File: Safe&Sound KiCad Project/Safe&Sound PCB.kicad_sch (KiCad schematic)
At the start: 14 parts

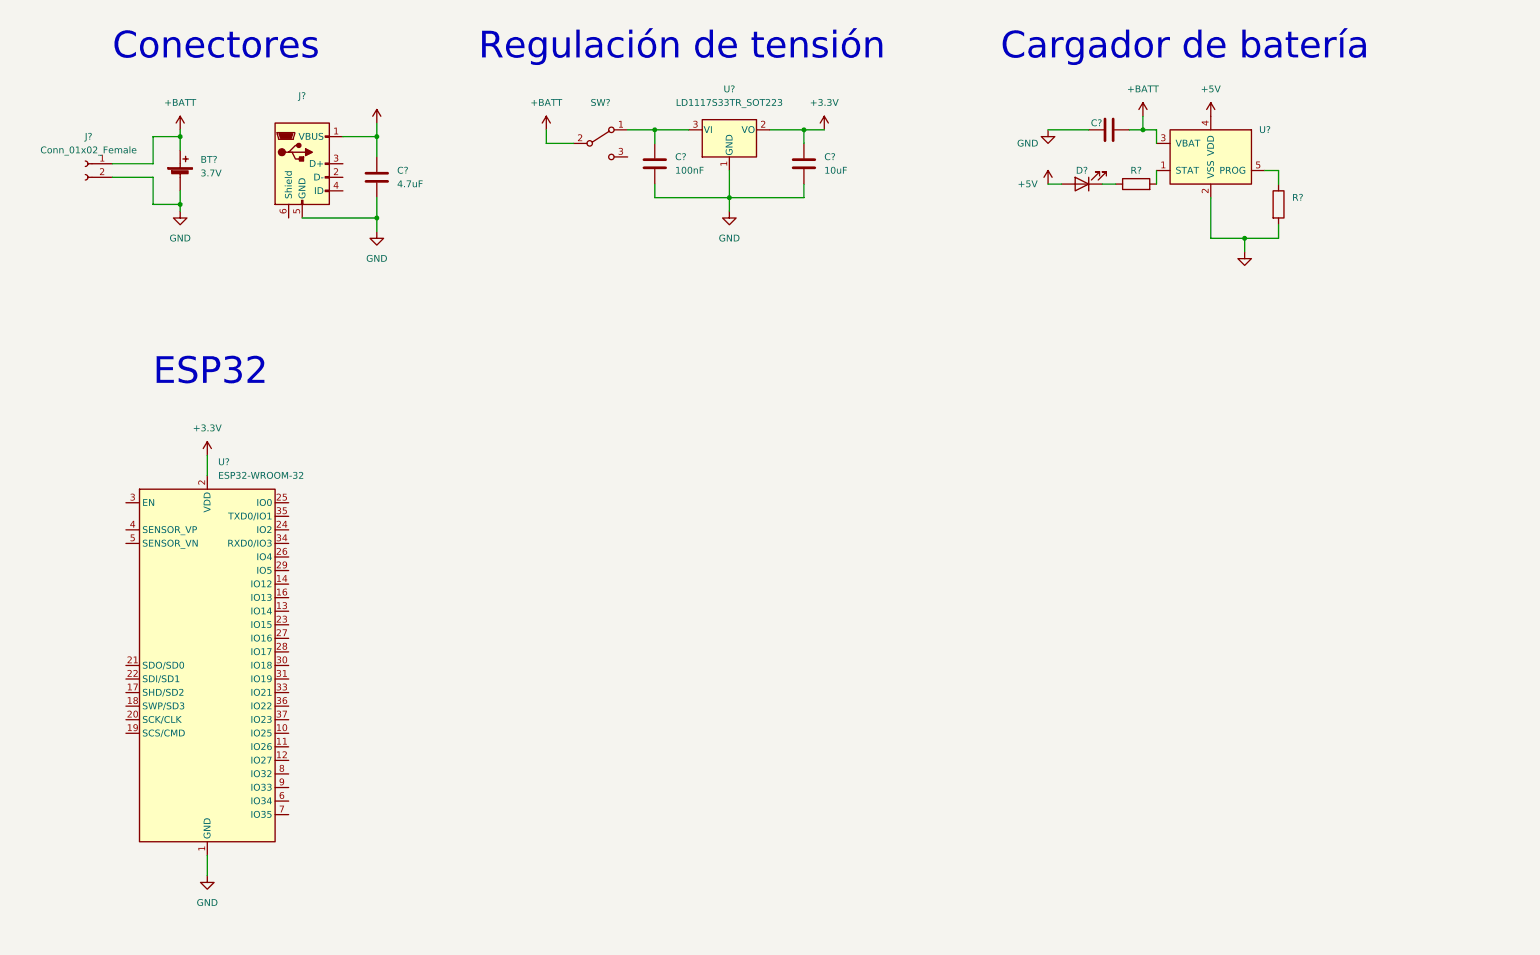
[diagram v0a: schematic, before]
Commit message: Puerto de programación
- Se añade un socket para hacer uso de un módulo USB a TTL con CP2102 para la programación del módulo ESP32-WROOM-32.
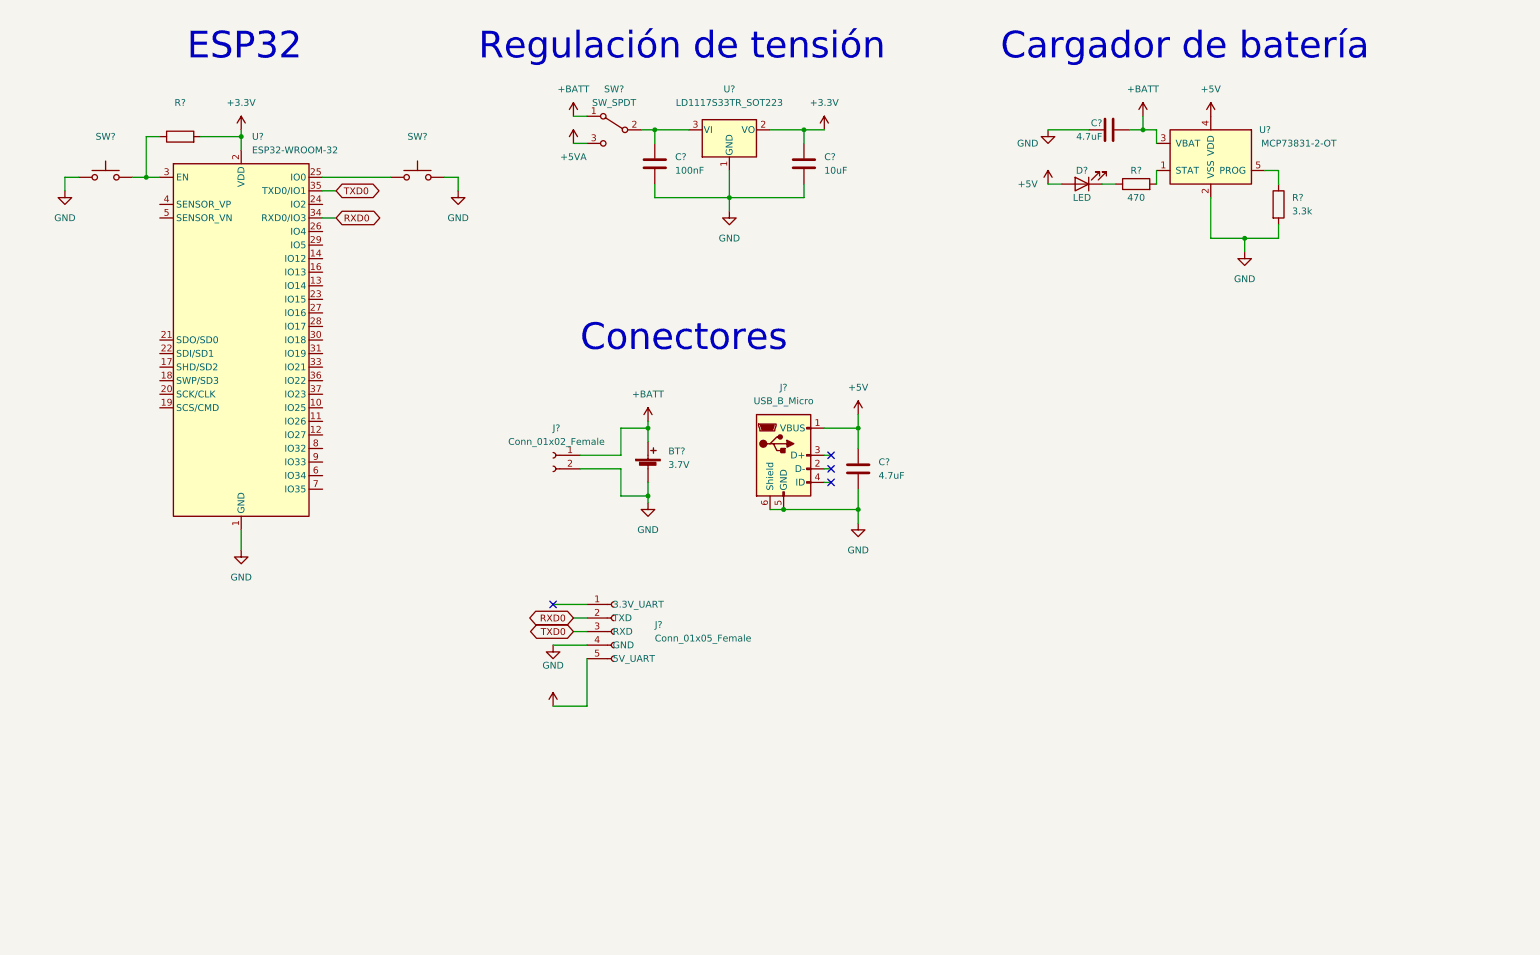
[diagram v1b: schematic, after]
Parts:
- added J?: Conn_01x05_Female, Connector_PinSocket_2.54mm:PinSocket_1x05_P2.54mm_Horizontal, symbol Connector:Conn_01x05_Female
- added R?: (no value), symbol Device:R
- added SW? (x2): (no value), symbol Switch:SW_Push
- C?: value (none) -> 4.7uF
- D?: value (none) -> LED
- J?: value (none) -> USB_B_Micro
- R?: value (none) -> 3.3k
- R?: value (none) -> 470
- SW?: value (none) -> SW_SPDT
- U?: value (none) -> MCP73831-2-OT; footprint (none) -> Package_TO_SOT_SMD:SOT-23-5
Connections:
- net +3V3: now also R?.2
- net +BATT: now also SW?.1 (A); no longer SW?.2 (B)
- net GND: now also J?.6 (Shield), J?.4 (GND), SW?.1, SW?.2
- net at U?.25 (IO0): now also SW?.1
- net at U?.3 (EN): now also R?.1, SW?.2
- net RXD0: now reaches U?.34 (RXD0/IO3)
- net RXD0: now also J?.2 (TXD)
- net TXD0: now reaches U?.35 (TXD0/IO1)
- net TXD0: now also J?.3 (RXD)
- net at C?.1, U?.3 (VI): now also SW?.2 (B); no longer SW?.1 (A)
- net +5VA: now reaches SW?.3 (C)
- net +5VA: now also J?.5 (5V_UART)
- no-connect marks 0 -> 4
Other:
- moved on the sheet: BT?, C?, J?, SW?, U?

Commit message: Acelerómetro y cambio regulador
- Se añada el conector de acelerómetro
- Se cambia el regulador LD1117 por el MCP1825 y se agrega a la librería del proyecto
- Se modifica el botón de GPIO0 para asegurar que se encuentre en pull-up externamente
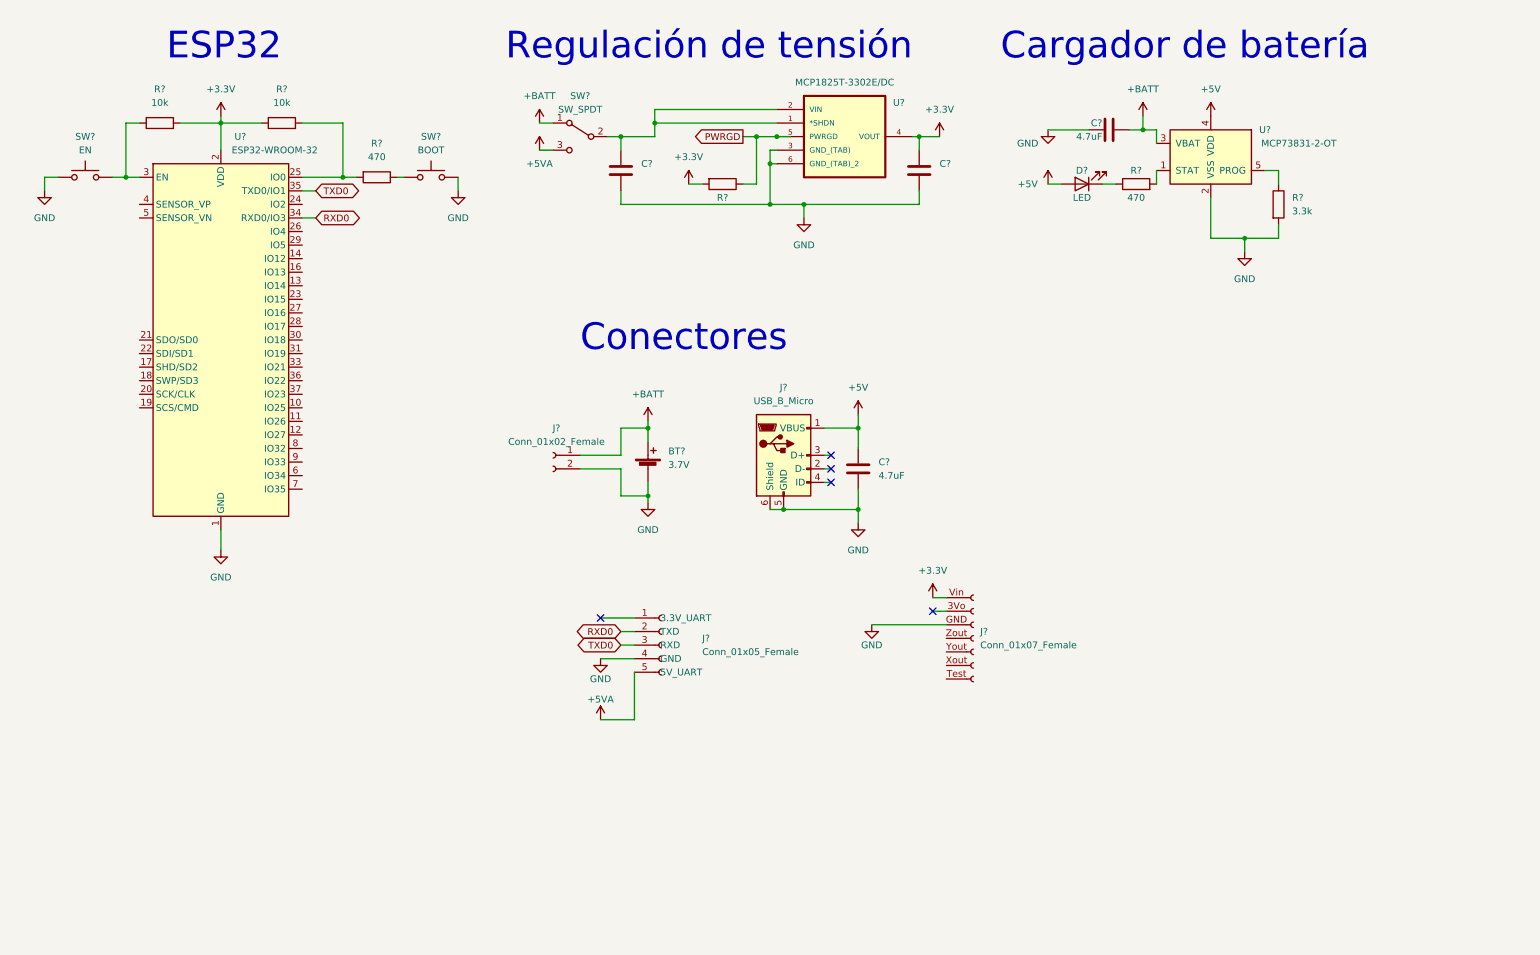
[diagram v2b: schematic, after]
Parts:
- removed U?: LD1117S33TR_SOT223, Package_TO_SOT_SMD:SOT-223-3_TabPin2, symbol Regulator_Linear:LD1117S33TR_SOT223
- added J?: Conn_01x07_Female, Connector_PinSocket_2.54mm:PinSocket_1x07_P2.54mm_Vertical, symbol Connector:Conn_01x07_Female
- added R?: 10k, symbol Device:R
- added R?: (no value), symbol Device:R
- added R?: 470, symbol Device:R
- added U?: MCP1825T-3302E/DC, SOT230P700X180-6N, symbol MCP1825T-3302E_DC:MCP1825T-3302E/DC
- C?: value 10uF -> (none)
- C?: value 100nF -> (none)
- R?: value (none) -> 10k
- SW?: value (none) -> BOOT
- SW?: value (none) -> EN
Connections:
- net +3V3: now also J?.Vin (Pin_1), R?.1, R?.2, U?.4 (VOUT)
- net GND: now also J?.GND (Pin_3), U?.3 (GND_(TAB)), U?.6 (GND_(TAB)_2)
- net at U?.25 (IO0): now also R?.2, R?.2; no longer SW?.1
- net at C?.1, SW?.2 (B): now also U?.1 (*SHDN), U?.2 (VIN)
- new net: R?.1, SW?.1
- new net PWRGD: R?.1, U?.5 (PWRGD)
- no-connect marks 4 -> 5
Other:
- moved on the sheet: C?, J?, R?, SW?, U?

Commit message: Asignación de huellas y correcciones
- Se realizan correcciones 
- Se agregan huellas provisionales de los componentes
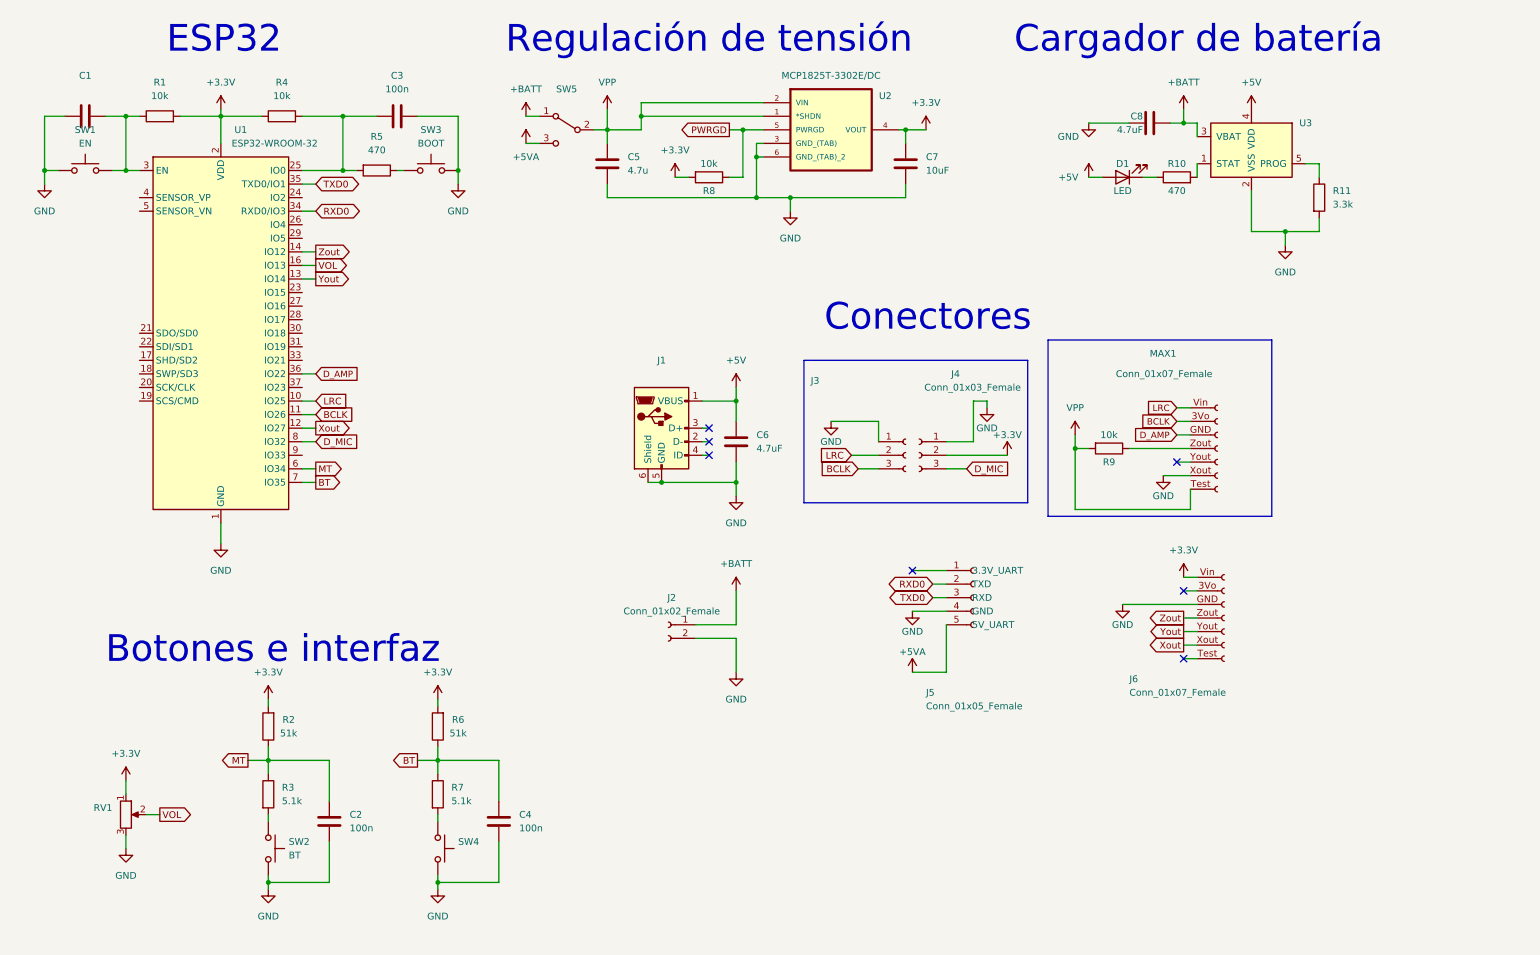
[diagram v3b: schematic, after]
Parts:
- removed BT?: 3.7V, symbol Device:Battery_Cell
- added C1: (no value), symbol Device:C
- added C2, C3, C4: 100n, symbol Device:C
- added J3: (no value), symbol Connector:Conn_01x03_Female
- added J4: Conn_01x03_Female, Connector_PinSocket_2.54mm:PinSocket_1x03_P2.54mm_Vertical, symbol Connector:Conn_01x03_Female
- added MAX1: Conn_01x07_Female, Connector_PinSocket_2.54mm:PinSocket_1x07_P2.54mm_Vertical, symbol Connector:Conn_01x07_Female
- added R2, R6: 51k, symbol Device:R
- added R3, R7: 5.1k, symbol Device:R
- added R9: 10k, symbol Device:R
- added RV1: (no value), symbol Device:R_Potentiometer
- added SW2: BT, symbol Switch:SW_Push
- added SW4: (no value), symbol Switch:SW_Push
- C5: renamed from C?; value (none) -> 4.7u
- C7: renamed from C?; value (none) -> 10uF
- J1: renamed from J?; value USB_B_Micro -> (none)
- R8: renamed from R?; value (none) -> 10k
- SW5: renamed from SW?; value SW_SPDT -> (none)
- U2: renamed from U?; footprint SOT230P700X180-6N -> (none)
- U3: renamed from U?; value MCP73831-2-OT -> (none); footprint Package_TO_SOT_SMD:SOT-23-5 -> (none)
- gave numbers to parts that had none: 14
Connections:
- net +3V3: now also J4.2 (Pin_2), R2.2, R6.2, RV1.1
- net GND: now also C1.1, C2.1, C3.2, C4.1, J3.1 (Pin_1), J4.1 (Pin_1), MAX1.Xout (Pin_6), RV1.3, SW2.2, SW4.2
- net VPP: now reaches C5.1, SW5.2 (B), U2.1 (*SHDN), U2.2 (VIN)
- net VPP: now also MAX1.Test (Pin_7), R9.2
- net at R1.1, SW1.2, U1.3 (EN): now also C1.2
- net LRC: now reaches U1.10 (IO25)
- net LRC: now also J3.2 (Pin_2), MAX1.Vin (Pin_1)
- net BCLK: now reaches U1.11 (IO26)
- net BCLK: now also J3.3 (Pin_3), MAX1.3Vo (Pin_2)
- net Xout: now reaches U1.12 (IO27)
- net Xout: now also J6.Xout (Pin_6)
- net Yout: now reaches U1.13 (IO14)
- net Yout: now also J6.Yout (Pin_5)
- net Zout: now reaches U1.14 (IO12)
- net Zout: now also J6.Zout (Pin_4)
- net VOL: now reaches U1.16 (IO13)
- net VOL: now also RV1.2
- net at R4.2, R5.2, U1.25 (IO0): now also C3.1
- net D_AMP: now reaches U1.36 (IO22)
- net D_AMP: now also MAX1.GND (Pin_3)
- net MT: now reaches U1.6 (IO34)
- net MT: now also C2.2, R2.1, R3.1
- net BT: now reaches U1.7 (IO35)
- net BT: now also C4.2, R6.1, R7.1
- net D_MIC: now reaches U1.8 (IO32)
- net D_MIC: now also J4.3 (Pin_3)
- new net: R7.2, SW4.1
- new net: MAX1.Zout (Pin_4), R9.1
- new net: R3.2, SW2.1
- no-connect marks 5 -> 7
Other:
- note added: "Botones e interfaz"
- moved on the sheet: C5, C6, C7, C8, D1, J1, J2, J5, J6, R1, R10, R11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

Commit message: Organización preliminar de componentes
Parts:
- C1: value (none) -> 100n; footprint (none) -> Capacitor_SMD:C_0805_2012Metric_Pad1.18x1.45mm_HandSolder
- C2, C3, C4, C5, C6, C7, C8: footprint (none) -> Capacitor_SMD:C_0805_2012Metric_Pad1.18x1.45mm_HandSolder
- D1: footprint (none) -> LED_SMD:LED_0805_2012Metric_Pad1.15x1.40mm_HandSolder
- J1: value (none) -> USB_B_Micro; footprint (none) -> Connector_USB:USB_Micro-B_Molex-105017-0001
- J3: value (none) -> Conn_01x03_Female; footprint (none) -> Connector_PinSocket_2.54mm:PinSocket_1x03_P2.54mm_Vertical
- J5: value Conn_01x05_Female -> (none); footprint Connector_PinSocket_2.54mm:PinSocket_1x05_P2.54mm_Horizontal -> (none)
- J6, MAX1: value Conn_01x07_Female -> (none); footprint Connector_PinSocket_2.54mm:PinSocket_1x07_P2.54mm_Vertical -> (none)
- R1, R10, R11, R2, R3, R4, R5, R6, R7, R8, R9: footprint (none) -> Resistor_SMD:R_0805_2012Metric_Pad1.20x1.40mm_HandSolder
- RV1: value (none) -> R_Potentiometer; footprint (none) -> Potentiometer_SMD:Potentiometer_ACP_CA6-VSMD_Vertical
- SW1, SW3: footprint (none) -> Button_Switch_SMD:SW_SPST_EVQQ2
- SW2: value BT -> (none); footprint (none) -> Button_Switch_SMD:SW_SPST_EVQQ2
- SW4: value (none) -> BT; footprint (none) -> Button_Switch_SMD:SW_SPST_EVQQ2
- SW5: value (none) -> SW_SPDT; footprint (none) -> Button_Switch_THT:SW_CuK_OS102011MA1QN1_SPDT_Angled
- U2: footprint (none) -> MCP1825T-3302E_DC:SOT230P700X180-6N
- U3: value (none) -> MCP73831-2-OT; footprint (none) -> Package_TO_SOT_SMD:SOT-23-5_HandSoldering
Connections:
- net +3V3: now also J6.1 (Pin_1); no longer J6.Vin (Pin_1)
- net BCLK: now also MAX1.2 (Pin_2); no longer MAX1.3Vo (Pin_2)
- net D_AMP: now also MAX1.3 (Pin_3); no longer MAX1.GND (Pin_3)
- net GND: now also J6.3 (Pin_3), MAX1.6 (Pin_6); no longer J6.GND (Pin_3), MAX1.Xout (Pin_6)
- net LRC: now also MAX1.1 (Pin_1); no longer MAX1.Vin (Pin_1)
- net VPP: now also MAX1.7 (Pin_7); no longer MAX1.Test (Pin_7)
- net Xout: now also J6.6 (Pin_6); no longer J6.Xout (Pin_6)
- net Yout: now also J6.5 (Pin_5); no longer J6.Yout (Pin_5)
- net Zout: now also J6.4 (Pin_4); no longer J6.Zout (Pin_4)
- net at R9.1: now also MAX1.4 (Pin_4); no longer MAX1.Zout (Pin_4)

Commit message: PCB y archivos de fabricación
- Se agrega el LED de usuario
- Se trazan las rutas de la PCB
- Se generan los archivos de fabricación
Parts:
- added D2: LED, LED_SMD:LED_0805_2012Metric_Pad1.15x1.40mm_HandSolder, symbol Device:LED
- J5: value (none) -> Conn_01x05_Female; footprint (none) -> Connector_PinSocket_2.54mm:PinSocket_1x05_P2.54mm_Horizontal
- J6, MAX1: value (none) -> Conn_01x07_Female; footprint (none) -> Connector_PinSocket_2.54mm:PinSocket_1x07_P2.54mm_Vertical
- R8: value 10k -> 470
- SW2: value (none) -> MT
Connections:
- net +3V3: no longer R8.2
- net GND: now also D2.1 (K)
- net LED: now reaches U1.24 (IO2)
- net LED: now also R8.2
- net PWRGD: no longer names the net of U2.5 (PWRGD)
- net PWRGD: no longer R8.1
- new net: D2.2 (A), R8.1
- no-connect marks 7 -> 8
